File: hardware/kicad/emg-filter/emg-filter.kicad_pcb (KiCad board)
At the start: 2 copper layers, 113.7 x 234.3 mm, 78 parts, among them J1 Conn_01x02, J10 Conn_01x02, J11 Conn_01x05, J12 Conn_01x02, J13 Conn_01x02, J14 Conn_01x05, J15 Conn_01x02, J16 Conn_01x02, J17 Conn_01x05, J18 Conn_01x02, J19 Conn_01x02, J2 Conn_01x03, J20 Conn_01x05, J21 Conn_01x02, J22 Conn_01x02, J23 Conn_01x05, J24 Conn_01x02, J25 Conn_01x02, J26 Conn_01x05, J27 Conn_01x02, J28 Conn_01x02, J29 Conn_01x02, J3 Conn_02x20_Odd_Even, J30 Conn_01x02, J31 Conn_01x02, J32 Conn_01x02, J33 Conn_01x02, J34 Conn_01x02, J35 Conn_01x02, J36 Conn_01x02, J37 Conn_01x02, J38 Conn_01x02, J39 Conn_01x02, J4 Conn_01x02, J40 Conn_01x02, J41 Conn_01x02, J5 Conn_01x05, J6 Conn_01x02, J7 Conn_01x02, J8 Conn_01x05, J9 Conn_01x02, U1 LM7805_TO220, U2 LM7905_TO220, U3 ADC108S102, U4 ADC108S102

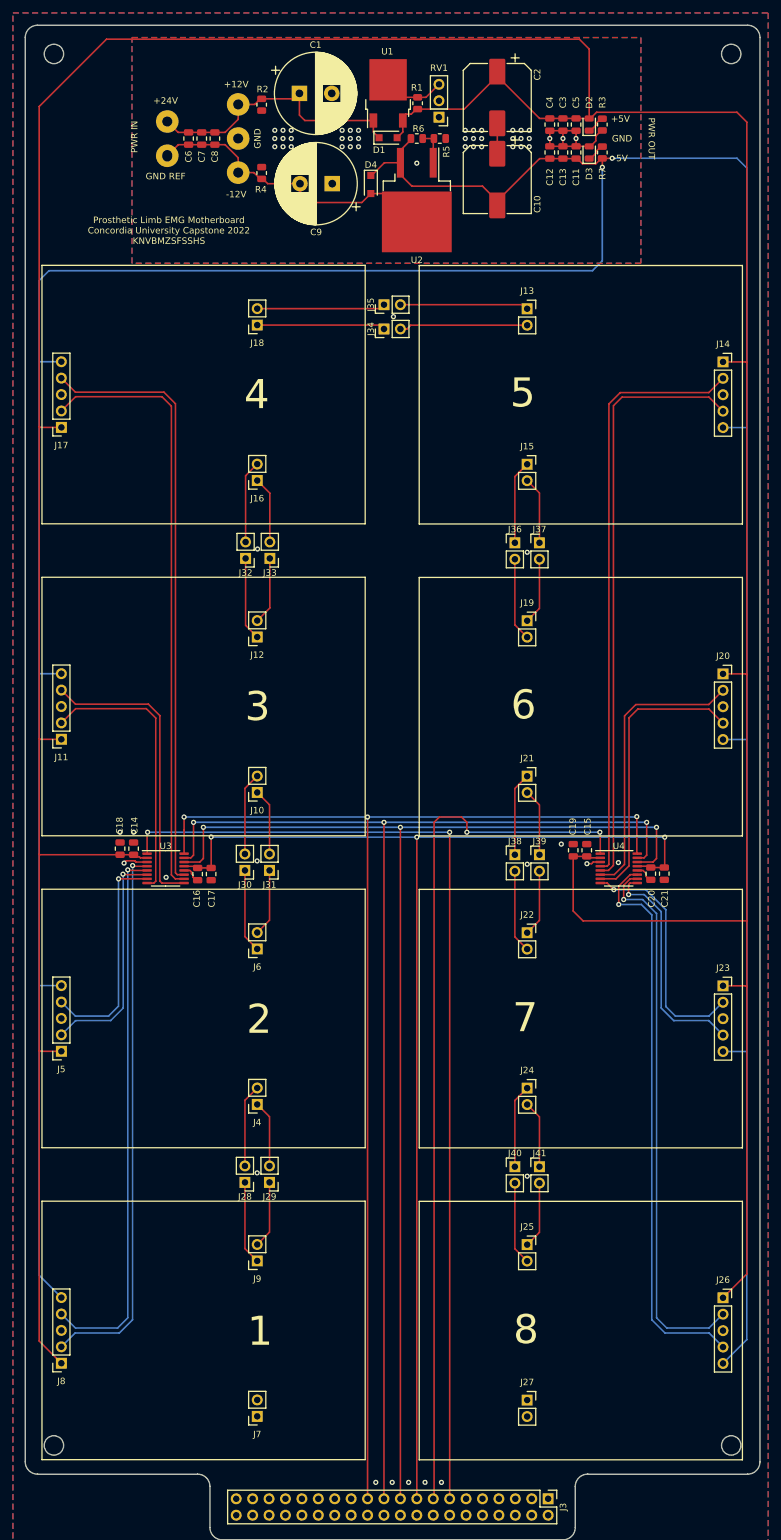
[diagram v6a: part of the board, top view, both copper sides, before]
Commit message: fixed power rails thickness
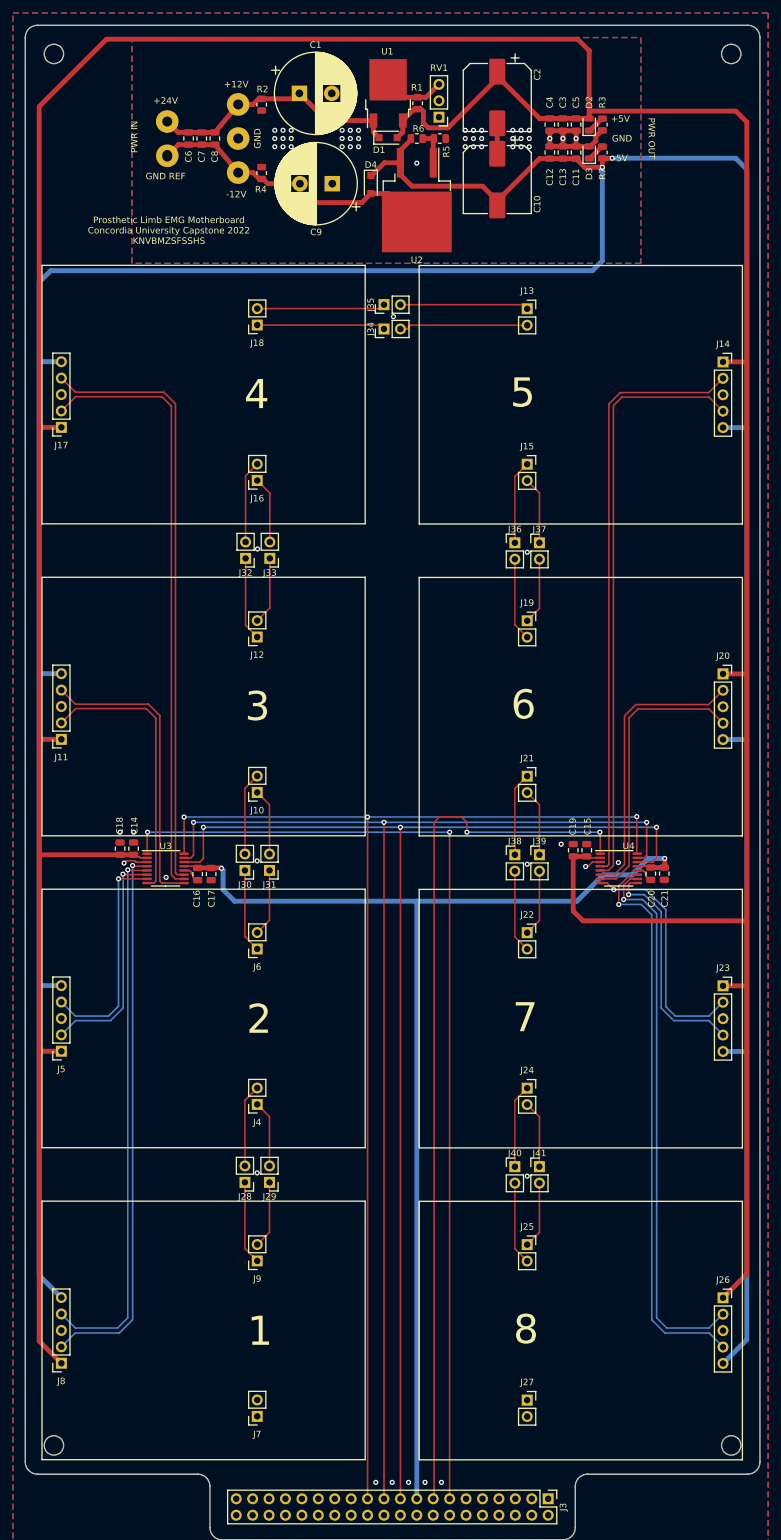
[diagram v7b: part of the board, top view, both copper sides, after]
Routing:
- net +3V3: track 190.7 -> 179.4 mm, vias 3 -> 2
- net +5V: track 623.5 -> 633.0 mm
- net -5V: track 544.2 -> 548.7 mm
- net +24V: track 43.2 -> 40.1 mm
- net GNDREF: track 48.0 -> 46.9 mm
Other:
- net class Power added: clearance 0.2, trace_width 0.75, via_dia 0.8, via_drill 0.4

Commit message: gerbers
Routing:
- net AGND: vias 59 -> 60
